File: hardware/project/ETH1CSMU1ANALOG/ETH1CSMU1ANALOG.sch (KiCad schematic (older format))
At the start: 0 parts

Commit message: Base board schematic.
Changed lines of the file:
@@
 $Descr A4 11693 8268
 encoding utf-8
-Sheet 1 5
+Sheet 1 6
 Title ""
 Date ""
@@
 F1 "MCU.sch" 50
 $EndSheet
+$Sheet
+S 8350 2650 1750 1500
+U 5F83EBF9
+F0 "Output module" 50
+F1 "Output_Module.sch" 50
+$EndSheet
 $EndSCHEMATC

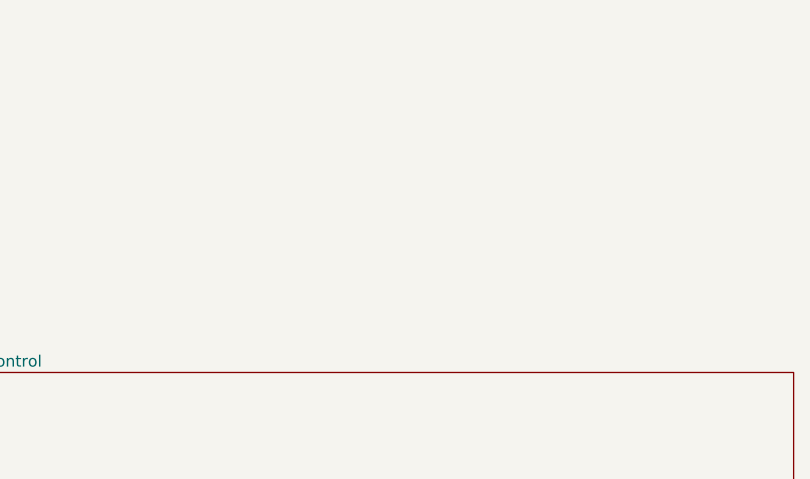
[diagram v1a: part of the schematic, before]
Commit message: Footprint assigment
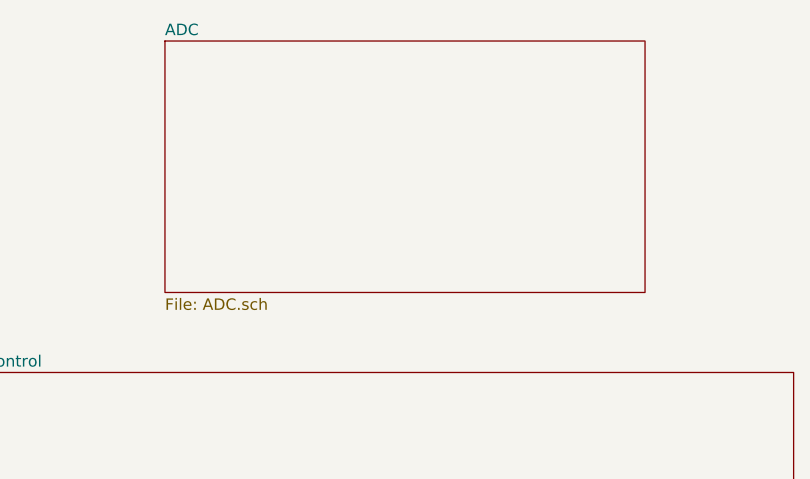
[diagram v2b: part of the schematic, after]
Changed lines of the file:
@@
 EESchema Schematic File Version 4
-LIBS:ETH1CSMU1ANALOG-cache
 EELAYER 30 0
 EELAYER END
 $Descr A4 11693 8268
 encoding utf-8
-Sheet 1 6
+Sheet 1 7
 Title ""
 Date ""
@@
 F1 "Output_Module.sch" 50
 $EndSheet
+$Sheet
+S 2350 850  2100 1100
+U 5E895799
+F0 "ADC" 50
+F1 "ADC.sch" 50
+$EndSheet
 $EndSCHEMATC

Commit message: Footprint assignment
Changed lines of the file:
@@
 $Descr A4 11693 8268
 encoding utf-8
-Sheet 1 7
+Sheet 1 9
 Title ""
 Date ""
@@
 $EndSheet
 $Sheet
-S 5300 5000 2450 1400
-U 5DB2ED13
-F0 "MCU" 50
-F1 "MCU.sch" 50
-$EndSheet
-$Sheet
 S 8350 2650 1750 1500
 U 5F83EBF9
@@
 F1 "ADC.sch" 50
 $EndSheet
+$Sheet
+S 5700 4900 2600 1050
+U 5E8AF09E
+F0 "MCU1" 50
+F1 "MCU1.sch" 50
+$EndSheet
+$Sheet
+S 8850 5000 1700 1100
+U 5E8BD814
+F0 "MCU2" 50
+F1 "MCU2.sch" 50
+$EndSheet
+$Sheet
+S 7100 1050 1450 650
+U 5E8BE911
+F0 "Trigger" 50
+F1 "Trigger.sch" 50
+$EndSheet
+$Sheet
+S 9200 1700 1400 700
+U 5E8BEA9C
+F0 "Ethernet" 50
+F1 "Ethernet.sch" 50
+$EndSheet
 $EndSCHEMATC
